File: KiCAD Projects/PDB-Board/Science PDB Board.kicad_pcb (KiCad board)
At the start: 2 copper layers, 2 parts

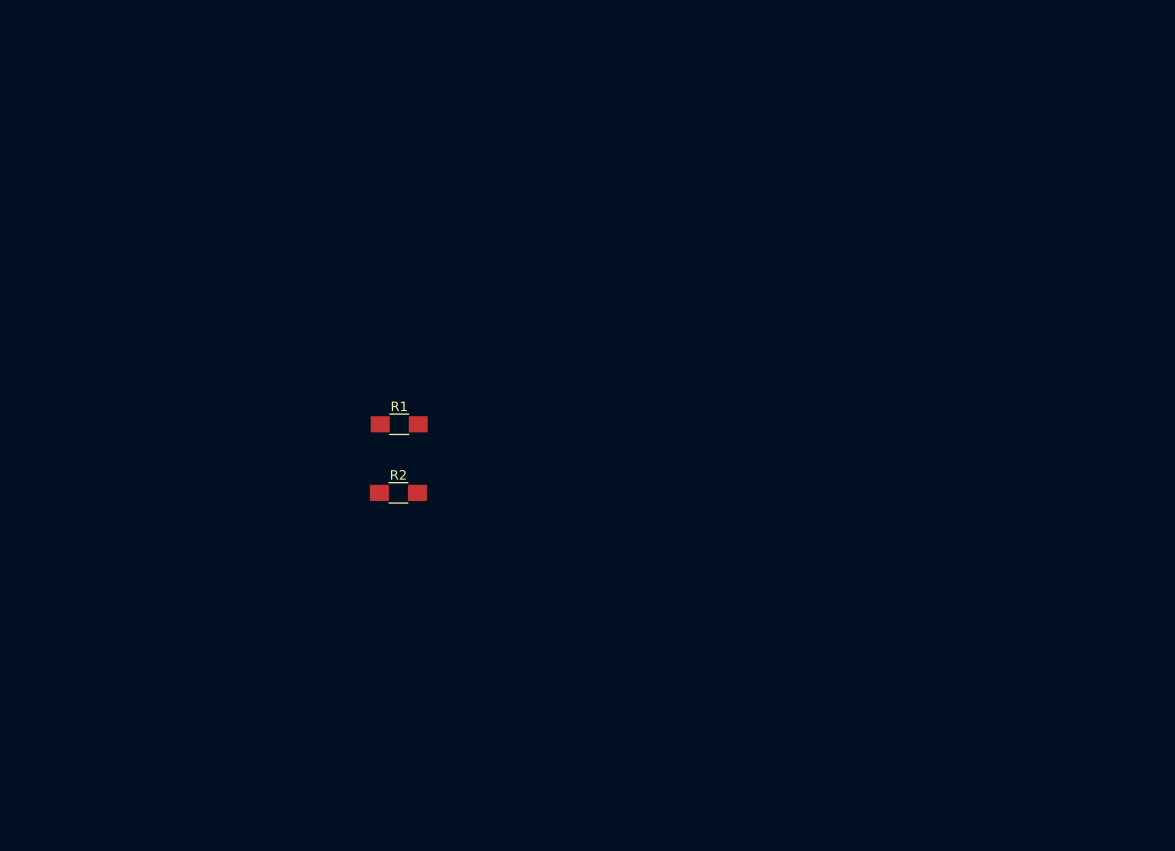
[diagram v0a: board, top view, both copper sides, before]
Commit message: Worked some more on Power Distribution Board
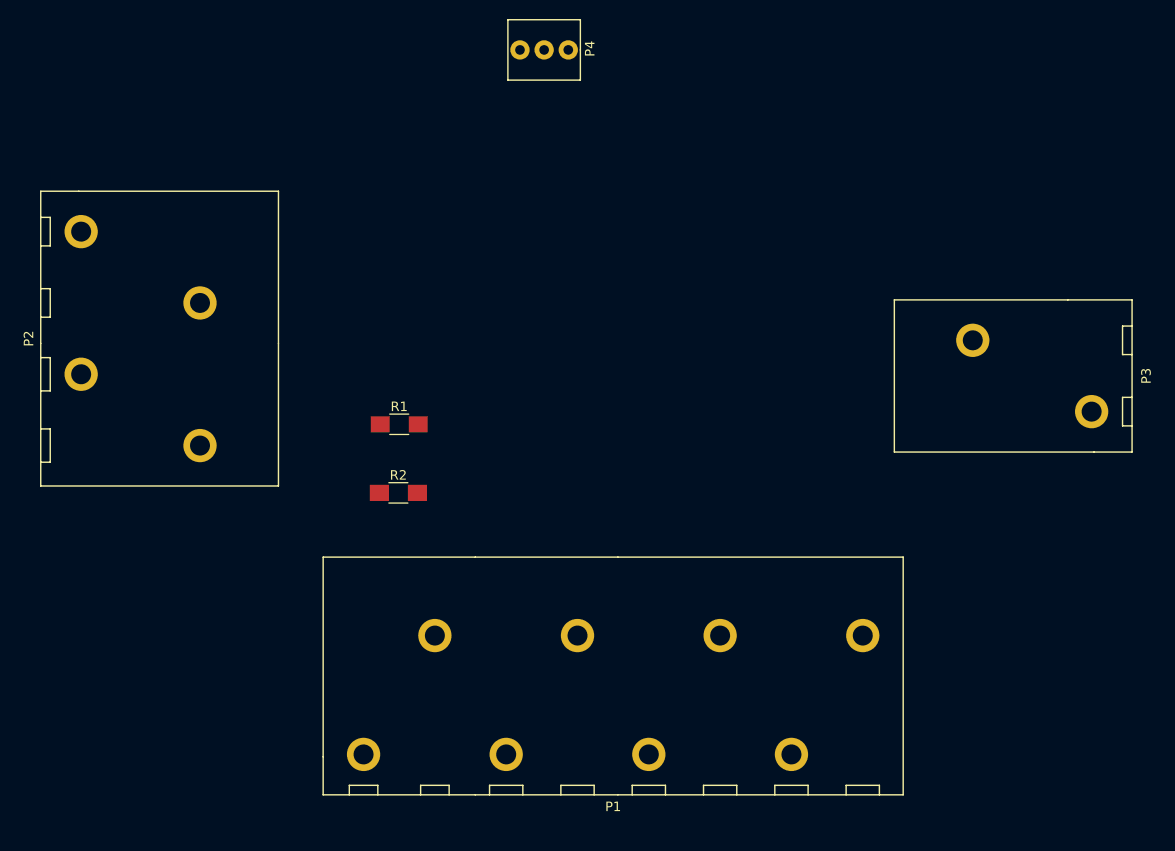
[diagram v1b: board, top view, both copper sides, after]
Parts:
- added P1: MOTOR_PWR_OUT, .pretty:PHOENIX_1792287, F.Cu at (148.6, 111.8)
- added P2: MAIN_PWR_IN, .pretty:PHOENIX_1792245, F.Cu at (135.9, 81.3)
- added P3: 5V_OUT, .pretty:PHOENIX_1792229, F.Cu at (200.7, 92.7)
- added P4: PWR_REG, .pretty:MOLEX_0022232031, F.Cu at (163.8, 58.4)
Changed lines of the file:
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@@
 (kicad_pcb (version 4) (host pcbnew 4.0.3-stable)
   (general
-    (links 0)
-    (no_connects 0)
-    (area 0 0 0 0)
+    (links 16)
+    (no_connects 16)
+    (area 123.804999 85.131 260.285001 141.875)
     (thickness 1.6)
     (drawings 0)
     (tracks 0)
     (zones 0)
-    (modules 2)
-    (nets 5)
+    (modules 6)
+    (nets 6)
   )
   (page A4)
@@
   (net 3 +5V)
   (net 4 "Net-(D2-Pad2)")
+  (net 5 GND)
   (net_class Default "This is the default net class."
     (clearance 0.2)
@@
     (add_net +12V)
     (add_net +5V)
+    (add_net GND)
     (add_net "Net-(D1-Pad2)")
     (add_net "Net-(D2-Pad2)")
@@
     )
   )
+  (module .pretty:PHOENIX_1792229 (layer F.Cu)
+    (at 200.66 92.71 90)
+    (fp_text reference P3 (at 0 26.5 90) (layer F.SilkS)
+      (effects (font (size 1 1) (thickness 0.15)))
+    )
+    (fp_text value 5V_OUT (at 0 1.25 90) (layer F.Fab)
+      (effects (font (size 1 1) (thickness 0.15)))
+    )
+    (fp_line (start -8 0) (end 8 0) (layer F.SilkS) (width 0.15))
+    (fp_line (start 2.25 25) (end 2.25 24) (layer F.SilkS) (width 0.15))
+    (fp_line (start 2.25 24) (end 5.25 24) (layer F.SilkS) (width 0.15))
+    (fp_line (start 5.25 24) (end 5.25 25) (layer F.SilkS) (width 0.15))
+    (fp_line (start -5.25 25) (end -5.25 24) (layer F.SilkS) (width 0.15))
+    (fp_line (start -5.25 24) (end -2.25 24) (layer F.SilkS) (width 0.15))
+    (fp_line (start -2.25 24) (end -2.25 25) (layer F.SilkS) (width 0.15))
+    (fp_line (start -8 21) (end -8 25) (layer F.SilkS) (width 0.15))
+    (fp_line (start -8 25) (end 8 25) (layer F.SilkS) (width 0.15))
+    (fp_line (start 8 25) (end 8 18.25) (layer F.SilkS) (width 0.15))
+    (fp_line (start 8 0) (end 8 18.25) (layer F.SilkS) (width 0.15))
+    (fp_line (start -8 21) (end -8 0) (layer F.SilkS) (width 0.15))
+    (pad 1 thru_hole circle (at -3.75 20.75 90) (size 3.5 3.5) (drill 2.1) (layers *.Cu *.Mask)
+      (net 5 GND))
+    (pad 2 thru_hole circle (at 3.75 8.25 90) (size 3.5 3.5) (drill 2.1) (layers *.Cu *.Mask)
+      (net 3 +5V))
+  )
+  (module .pretty:PHOENIX_1792245 (layer F.Cu)
+    (at 135.89 81.28 270)
+    (fp_text reference P2 (at 7.5 26.25 270) (layer F.SilkS)
+      (effects (font (size 1 1) (thickness 0.15)))
+    )
+    (fp_text value MAIN_PWR_IN (at 7.5 1 270) (layer F.Fab)
+      (effects (font (size 1 1) (thickness 0.15)))
+    )
+    (fp_line (start 17 25) (end 17 24) (layer F.SilkS) (width 0.15))
+    (fp_line (start 17 24) (end 20.5 24) (layer F.SilkS) (width 0.15))
+    (fp_line (start 20.5 24) (end 20.5 25) (layer F.SilkS) (width 0.15))
+    (fp_line (start 9.5 25) (end 9.5 24) (layer F.SilkS) (width 0.15))
+    (fp_line (start 9.5 24) (end 13 24) (layer F.SilkS) (width 0.15))
+    (fp_line (start 13 24) (end 13 25) (layer F.SilkS) (width 0.15))
+    (fp_line (start 8 0) (end 23 0) (layer F.SilkS) (width 0.15))
+    (fp_line (start 23 0) (end 23 25) (layer F.SilkS) (width 0.15))
+    (fp_line (start 23 25) (end 8 25) (layer F.SilkS) (width 0.15))
+    (fp_line (start -8 0) (end 8 0) (layer F.SilkS) (width 0.15))
+    (fp_line (start 2.25 25) (end 2.25 24) (layer F.SilkS) (width 0.15))
+    (fp_line (start 2.25 24) (end 5.25 24) (layer F.SilkS) (width 0.15))
+    (fp_line (start 5.25 24) (end 5.25 25) (layer F.SilkS) (width 0.15))
+    (fp_line (start -5.25 25) (end -5.25 24) (layer F.SilkS) (width 0.15))
+    (fp_line (start -5.25 24) (end -2.25 24) (layer F.SilkS) (width 0.15))
+    (fp_line (start -2.25 24) (end -2.25 25) (layer F.SilkS) (width 0.15))
+    (fp_line (start -8 21) (end -8 25) (layer F.SilkS) (width 0.15))
+    (fp_line (start -8 25) (end 8 25) (layer F.SilkS) (width 0.15))
+    (fp_line (start -8 21) (end -8 0) (layer F.SilkS) (width 0.15))
+    (pad 1 thru_hole circle (at -3.75 20.75 270) (size 3.5 3.5) (drill 2.1) (layers *.Cu *.Mask)
+      (net 1 +12V))
+    (pad 2 thru_hole circle (at 3.75 8.25 270) (size 3.5 3.5) (drill 2.1) (layers *.Cu *.Mask)
+      (net 1 +12V))
+    (pad 3 thru_hole circle (at 11.25 20.75 270) (size 3.5 3.5) (drill 2.1) (layers *.Cu *.Mask)
+      (net 5 GND))
+    (pad 4 thru_hole circle (at 18.75 8.25 270) (size 3.5 3.5) (drill 2.1) (layers *.Cu *.Mask)
+      (net 5 GND))
+  )
+  (module .pretty:PHOENIX_1792287 (layer F.Cu)
+    (at 148.59 111.76)
+    (fp_text reference P1 (at 22.5 26.25) (layer F.SilkS)
+      (effects (font (size 1 1) (thickness 0.15)))
+    )
+    (fp_text value MOTOR_PWR_OUT (at 22.5 1.25) (layer F.Fab)
+      (effects (font (size 1 1) (thickness 0.15)))
+    )
+    (fp_line (start 47 25) (end 47 24) (layer F.SilkS) (width 0.15))
+    (fp_line (start 47 24) (end 50.5 24) (layer F.SilkS) (width 0.15))
+    (fp_line (start 50.5 24) (end 50.5 25) (layer F.SilkS) (width 0.15))
+    (fp_line (start 39.5 25) (end 39.5 24) (layer F.SilkS) (width 0.15))
+    (fp_line (start 39.5 24) (end 43 24) (layer F.SilkS) (width 0.15))
+    (fp_line (start 43 24) (end 43 25) (layer F.SilkS) (width 0.15))
+    (fp_line (start 32 25) (end 32 24) (layer F.SilkS) (width 0.15))
+    (fp_line (start 32 24) (end 35.5 24) (layer F.SilkS) (width 0.15))
+    (fp_line (start 35.5 24) (end 35.5 25) (layer F.SilkS) (width 0.15))
+    (fp_line (start 24.5 25) (end 24.5 24) (layer F.SilkS) (width 0.15))
+    (fp_line (start 24.5 24) (end 28 24) (layer F.SilkS) (width 0.15))
+    (fp_line (start 28 24) (end 28 25) (layer F.SilkS) (width 0.15))
+    (fp_line (start 23 0) (end 53 0) (layer F.SilkS) (width 0.15))
+    (fp_line (start 53 25) (end 23 25) (layer F.SilkS) (width 0.15))
+    (fp_line (start 53 0) (end 53 25) (layer F.SilkS) (width 0.15))
+    (fp_line (start 17 25) (end 17 24) (layer F.SilkS) (width 0.15))
+    (fp_line (start 17 24) (end 20.5 24) (layer F.SilkS) (width 0.15))
+    (fp_line (start 20.5 24) (end 20.5 25) (layer F.SilkS) (width 0.15))
+    (fp_line (start 9.5 25) (end 9.5 24) (layer F.SilkS) (width 0.15))
+    (fp_line (start 9.5 24) (end 13 24) (layer F.SilkS) (width 0.15))
+    (fp_line (start 13 24) (end 13 25) (layer F.SilkS) (width 0.15))
+    (fp_line (start 8 0) (end 23 0) (layer F.SilkS) (width 0.15))
+    (fp_line (start 23 25) (end 8 25) (layer F.SilkS) (width 0.15))
+    (fp_line (start -8 0) (end 8 0) (layer F.SilkS) (width 0.15))
+    (fp_line (start 2.25 25) (end 2.25 24) (layer F.SilkS) (width 0.15))
+    (fp_line (start 2.25 24) (end 5.25 24) (layer F.SilkS) (width 0.15))
+    (fp_line (start 5.25 24) (end 5.25 25) (layer F.SilkS) (width 0.15))
+    (fp_line (start -5.25 25) (end -5.25 24) (layer F.SilkS) (width 0.15))
+    (fp_line (start -5.25 24) (end -2.25 24) (layer F.SilkS) (width 0.15))
+    (fp_line (start -2.25 24) (end -2.25 25) (layer F.SilkS) (width 0.15))
+    (fp_line (start -8 21) (end -8 25) (layer F.SilkS) (width 0.15))
+    (fp_line (start -8 25) (end 8 25) (layer F.SilkS) (width 0.15))
+    (fp_line (start -8 21) (end -8 0) (layer F.SilkS) (width 0.15))
+    (pad 1 thru_hole circle (at -3.75 20.75) (size 3.5 3.5) (drill 2.1) (layers *.Cu *.Mask)
+      (net 5 GND))
+    (pad 2 thru_hole circle (at 3.75 8.25) (size 3.5 3.5) (drill 2.1) (layers *.Cu *.Mask)
+      (net 1 +12V))
+    (pad 3 thru_hole circle (at 11.25 20.75) (size 3.5 3.5) (drill 2.1) (layers *.Cu *.Mask)
+      (net 5 GND))
+    (pad 4 thru_hole circle (at 18.75 8.25) (size 3.5 3.5) (drill 2.1) (layers *.Cu *.Mask)
+      (net 1 +12V))
+    (pad 5 thru_hole circle (at 26.25 20.75) (size 3.5 3.5) (drill 2.1) (layers *.Cu *.Mask)
+      (net 5 GND))
+    (pad 6 thru_hole circle (at 33.75 8.25) (size 3.5 3.5) (drill 2.1) (layers *.Cu *.Mask)
+      (net 1 +12V))
+    (pad 7 thru_hole circle (at 41.25 20.75) (size 3.5 3.5) (drill 2.1) (layers *.Cu *.Mask)
+      (net 5 GND))
+    (pad 8 thru_hole circle (at 48.75 8.25) (size 3.5 3.5) (drill 2.1) (layers *.Cu *.Mask)
+      (net 1 +12V))
+  )
+  (module .pretty:MOLEX_0022232031 (layer F.Cu)
+    (at 163.83 58.42)
+    (fp_text reference P4 (at 4.826 -0.127 90) (layer F.SilkS)
+      (effects (font (size 1 1) (thickness 0.15)))
+    )
+    (fp_text value PWR_REG (at 0 -4.064) (layer F.Fab)
+      (effects (font (size 1 1) (thickness 0.15)))
+    )
+    (fp_line (start 3.81 0) (end 3.81 3.175) (layer F.SilkS) (width 0.15))
+    (fp_line (start 3.81 3.175) (end -3.81 3.175) (layer F.SilkS) (width 0.15))
+    (fp_line (start -3.81 3.175) (end -3.81 -3.175) (layer F.SilkS) (width 0.15))
+    (fp_line (start -3.81 -3.175) (end 3.81 -3.175) (layer F.SilkS) (width 0.15))
+    (fp_line (start 3.81 -3.175) (end 3.81 0) (layer F.SilkS) (width 0.15))
+    (pad 2 thru_hole circle (at 0 0) (size 2.032 2.032) (drill 1.016) (layers *.Cu *.Mask)
+      (net 5 GND))
+    (pad 1 thru_hole circle (at -2.54 0) (size 2.032 2.032) (drill 1.016) (layers *.Cu *.Mask)
+      (net 1 +12V))
+    (pad 3 thru_hole circle (at 2.54 0) (size 2.032 2.032) (drill 1.016) (layers *.Cu *.Mask)
+      (net 3 +5V))
+  )
 )

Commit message: Worked on PDB PCB
Still needs mounting holes.
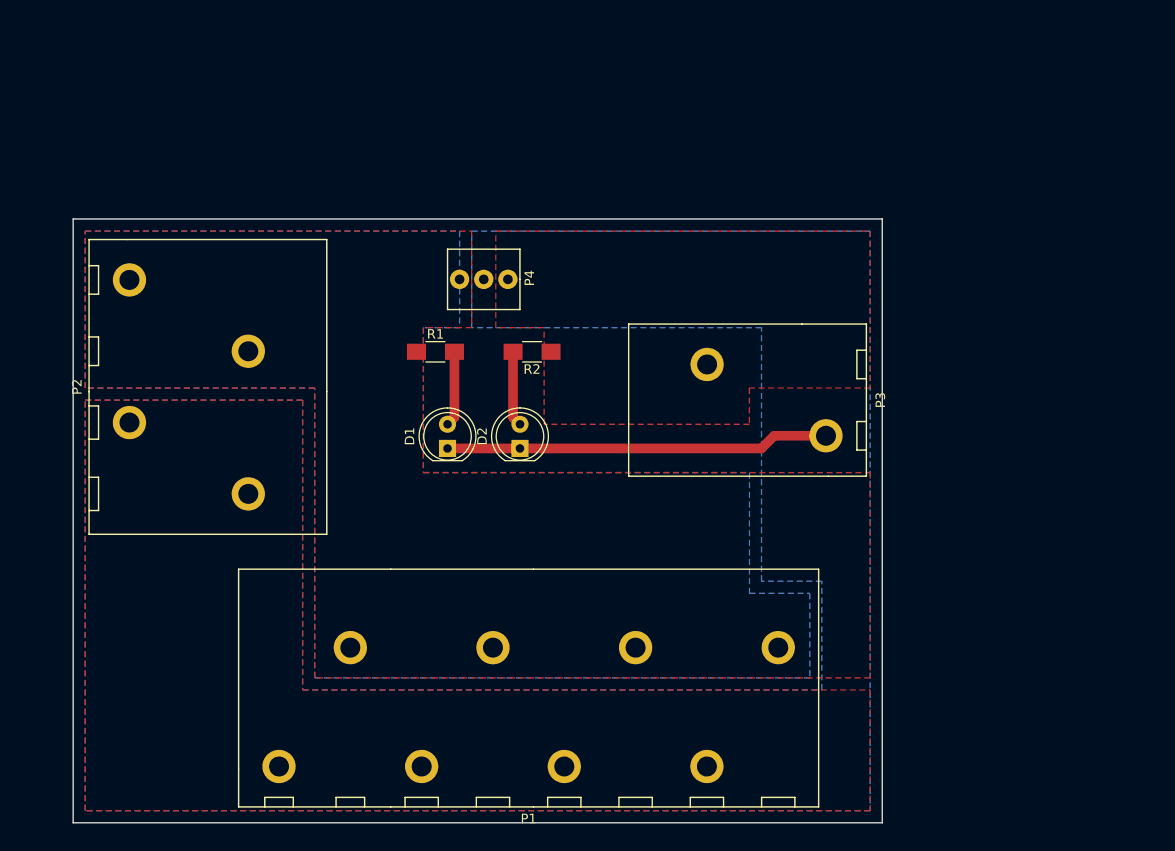
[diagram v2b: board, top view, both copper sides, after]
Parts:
- added D1: LED, LEDs:LED_D5.0mm, F.Cu at (153.7, 100.3)
- added D2: LED, LEDs:LED_D5.0mm, F.Cu at (161.3, 100.3)
- moved P3 28.1 mm to (172.7, 95.2)
- moved P4 25.0 mm to (157.5, 82.5)
- moved R2 20.4 mm to (162.6, 90.2), turned to 180 degrees
- moved P1 8.98 mm to (139.7, 113.0)
- moved R1 8.52 mm to (152.4, 90.2)
- moved P2 7.18 mm to (141.0, 86.4)
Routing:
- net GND: track 0.00 -> 40.4 mm
- net Net-(D1-Pad2): track 0.00 -> 7.92 mm
- net Net-(D2-Pad2): track 0.00 -> 7.92 mm
- added copper zone on B.Cu, net +12V
- added copper zone on F.Cu, net +12V
- added copper zone on F.Cu, net +5V
- added copper zone on B.Cu, net GND
- added copper zone on F.Cu, net GND
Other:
- board outline added: 85.1 x 63.5 mm

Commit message: Finished? PDB v2
Committing this that weren't?
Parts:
- added HL1: HOLE, hole:HOLE_M3, F.Cu at (144.8, 80.0)
- added HL2: HOLE, hole:HOLE_M3, F.Cu at (195.6, 80.0)
- added HL3: HOLE, hole:HOLE_M3, F.Cu at (119.4, 135.9)
- added HL4: HOLE, hole:HOLE_M3, F.Cu at (195.6, 135.9)
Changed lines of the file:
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@@
 (kicad_pcb (version 4) (host pcbnew 4.0.3-stable)
   (general
-    (links 20)
-    (no_connects 0)
+    (links 24)
+    (no_connects 1)
     (area 114.224999 76.124999 199.465001 139.775001)
     (thickness 1.6)
@@
     (tracks 8)
     (zones 0)
-    (modules 8)
+    (modules 12)
     (nets 6)
   )
@@
   )
   (setup
-    (last_trace_width 1.016)
+    (last_trace_width 0.25)
     (user_trace_width 1.016)
     (trace_clearance 0.2)
@@
     )
   )
+  (module hole:HOLE_M3 (layer F.Cu)
+    (at 144.78 80.01)
+    (fp_text reference HL1 (at -0.127 3.683) (layer F.SilkS)
+      (effects (font (size 1 1) (thickness 0.15)))
+    )
+    (fp_text value HOLE (at 0.127 -3.683) (layer F.Fab)
+      (effects (font (size 1 1) (thickness 0.15)))
+    )
+    (pad 1 thru_hole circle (at 0 0) (size 5 5) (drill 3.1) (layers *.Cu *.Mask)
+      (net 5 GND))
+  )
+  (module hole:HOLE_M3 (layer F.Cu)
+    (at 195.58 80.01)
+    (fp_text reference HL2 (at -0.127 3.683) (layer F.SilkS)
+      (effects (font (size 1 1) (thickness 0.15)))
+    )
+    (fp_text value HOLE (at 0.127 -3.683) (layer F.Fab)
+      (effects (font (size 1 1) (thickness 0.15)))
+    )
+    (pad 1 thru_hole circle (at 0 0) (size 5 5) (drill 3.1) (layers *.Cu *.Mask)
+      (net 5 GND))
+  )
+  (module hole:HOLE_M3 (layer F.Cu)
+    (at 119.38 135.89)
+    (fp_text reference HL3 (at -0.127 3.683) (layer F.SilkS)
+      (effects (font (size 1 1) (thickness 0.15)))
+    )
+    (fp_text value HOLE (at 0.127 -3.683) (layer F.Fab)
+      (effects (font (size 1 1) (thickness 0.15)))
+    )
+    (pad 1 thru_hole circle (at 0 0) (size 5 5) (drill 3.1) (layers *.Cu *.Mask)
+      (net 5 GND))
+  )
+  (module hole:HOLE_M3 (layer F.Cu)
+    (at 195.58 135.89)
+    (fp_text reference HL4 (at -0.127 3.683) (layer F.SilkS)
+      (effects (font (size 1 1) (thickness 0.15)))
+    )
+    (fp_text value HOLE (at 0.127 -3.683) (layer F.Fab)
+      (effects (font (size 1 1) (thickness 0.15)))
+    )
+    (pad 1 thru_hole circle (at 0 0) (size 5 5) (drill 3.1) (layers *.Cu *.Mask)
+      (net 5 GND))
+  )
   (gr_line (start 114.3 139.7) (end 114.3 76.2) (angle 90) (layer Edge.Cuts) (width 0.15))
   (gr_line (start 199.39 139.7) (end 114.3 139.7) (angle 90) (layer Edge.Cuts) (width 0.15))
@@
   (segment (start 160.56 90.17) (end 160.56 97.06) (width 1.016) (layer F.Cu) (net 4))
   (segment (start 160.56 97.06) (end 161.29 97.79) (width 1.016) (layer F.Cu) (net 4))
-  (segment (start 153.67 100.33) (end 161.29 100.33) (width 1.016) (layer F.Cu) (net 5) (status C00000))
-  (segment (start 161.29 100.33) (end 186.69 100.33) (width 1.016) (layer F.Cu) (net 5) (status 400000))
+  (segment (start 153.67 100.33) (end 161.29 100.33) (width 1.016) (layer F.Cu) (net 5))
+  (segment (start 161.29 100.33) (end 186.69 100.33) (width 1.016) (layer F.Cu) (net 5))
   (segment (start 186.69 100.33) (end 188.02 99) (width 1.016) (layer F.Cu) (net 5))
-  (segment (start 188.02 99) (end 193.47 99) (width 1.016) (layer F.Cu) (net 5) (status 800000))
+  (segment (start 188.02 99) (end 193.47 99) (width 1.016) (layer F.Cu) (net 5))
   (zone (net 3) (net_name +5V) (layer F.Cu) (hatch edge 0.508)
     (connect_pads (clearance 0.508))

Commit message: Revert "Finished? PDB v2"
This reverts commit a04adeda8b22dfbdd33fba7944ab085dcccc9394.
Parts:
- removed HL1, HL2, HL3, HL4: HOLE, hole:HOLE_M3
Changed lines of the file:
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@@
 (kicad_pcb (version 4) (host pcbnew 4.0.3-stable)
   (general
-    (links 24)
-    (no_connects 1)
+    (links 20)
+    (no_connects 0)
     (area 114.224999 76.124999 199.465001 139.775001)
     (thickness 1.6)
@@
     (tracks 8)
     (zones 0)
-    (modules 12)
+    (modules 8)
     (nets 6)
   )
@@
   )
   (setup
-    (last_trace_width 0.25)
+    (last_trace_width 1.016)
     (user_trace_width 1.016)
     (trace_clearance 0.2)
@@
     )
   )
-  (module hole:HOLE_M3 (layer F.Cu)
-    (at 144.78 80.01)
-    (fp_text reference HL1 (at -0.127 3.683) (layer F.SilkS)
-      (effects (font (size 1 1) (thickness 0.15)))
-    )
-    (fp_text value HOLE (at 0.127 -3.683) (layer F.Fab)
-      (effects (font (size 1 1) (thickness 0.15)))
-    )
-    (pad 1 thru_hole circle (at 0 0) (size 5 5) (drill 3.1) (layers *.Cu *.Mask)
-      (net 5 GND))
-  )
-  (module hole:HOLE_M3 (layer F.Cu)
-    (at 195.58 80.01)
-    (fp_text reference HL2 (at -0.127 3.683) (layer F.SilkS)
-      (effects (font (size 1 1) (thickness 0.15)))
-    )
-    (fp_text value HOLE (at 0.127 -3.683) (layer F.Fab)
-      (effects (font (size 1 1) (thickness 0.15)))
-    )
-    (pad 1 thru_hole circle (at 0 0) (size 5 5) (drill 3.1) (layers *.Cu *.Mask)
-      (net 5 GND))
-  )
-  (module hole:HOLE_M3 (layer F.Cu)
-    (at 119.38 135.89)
-    (fp_text reference HL3 (at -0.127 3.683) (layer F.SilkS)
-      (effects (font (size 1 1) (thickness 0.15)))
-    )
-    (fp_text value HOLE (at 0.127 -3.683) (layer F.Fab)
-      (effects (font (size 1 1) (thickness 0.15)))
-    )
-    (pad 1 thru_hole circle (at 0 0) (size 5 5) (drill 3.1) (layers *.Cu *.Mask)
-      (net 5 GND))
-  )
-  (module hole:HOLE_M3 (layer F.Cu)
-    (at 195.58 135.89)
-    (fp_text reference HL4 (at -0.127 3.683) (layer F.SilkS)
-      (effects (font (size 1 1) (thickness 0.15)))
-    )
-    (fp_text value HOLE (at 0.127 -3.683) (layer F.Fab)
-      (effects (font (size 1 1) (thickness 0.15)))
-    )
-    (pad 1 thru_hole circle (at 0 0) (size 5 5) (drill 3.1) (layers *.Cu *.Mask)
-      (net 5 GND))
-  )
   (gr_line (start 114.3 139.7) (end 114.3 76.2) (angle 90) (layer Edge.Cuts) (width 0.15))
   (gr_line (start 199.39 139.7) (end 114.3 139.7) (angle 90) (layer Edge.Cuts) (width 0.15))
@@
   (segment (start 160.56 90.17) (end 160.56 97.06) (width 1.016) (layer F.Cu) (net 4))
   (segment (start 160.56 97.06) (end 161.29 97.79) (width 1.016) (layer F.Cu) (net 4))
-  (segment (start 153.67 100.33) (end 161.29 100.33) (width 1.016) (layer F.Cu) (net 5))
-  (segment (start 161.29 100.33) (end 186.69 100.33) (width 1.016) (layer F.Cu) (net 5))
+  (segment (start 153.67 100.33) (end 161.29 100.33) (width 1.016) (layer F.Cu) (net 5) (status C00000))
+  (segment (start 161.29 100.33) (end 186.69 100.33) (width 1.016) (layer F.Cu) (net 5) (status 400000))
   (segment (start 186.69 100.33) (end 188.02 99) (width 1.016) (layer F.Cu) (net 5))
-  (segment (start 188.02 99) (end 193.47 99) (width 1.016) (layer F.Cu) (net 5))
+  (segment (start 188.02 99) (end 193.47 99) (width 1.016) (layer F.Cu) (net 5) (status 800000))
   (zone (net 3) (net_name +5V) (layer F.Cu) (hatch edge 0.508)
     (connect_pads (clearance 0.508))
